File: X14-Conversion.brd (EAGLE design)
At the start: 50.8 x 76.2 mm, 23 parts, among them P1 282837-2, P2 282837-2, P3 282837-2

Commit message: Complete Board Layout
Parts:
- C3: device SparkFun-Capacitors:0402 -> SparkFun-Capacitors:0603
- CB: value 10nF 0Ω -> 10NF-0603-50V-10%
- CONN: value DISTRIBUTION-CONVERSION -> CONVERSION-DISTRIBUTION; device CONN, Distribution-Conversion:TSW-105-05-G-S -> CONN, Distribution-Conversion (3):TSW-105-05-G-S(C-D)
- moved U$7 69.9 mm to (63.0, 44.8)
- moved U$6 67.3 mm to (63.8, 41.5)
- moved U$5 64.1 mm to (63.5, 38.0)
- moved P3 62.9 mm to (7.49, 69.8), turned to 180 degrees
- moved U$4 61.3 mm to (65.2, 28.7)
- moved U$3 61.3 mm to (64.9, 32.0)
- moved U$2 61.1 mm to (64.6, 34.8)
- moved COUT 38.2 mm to (30.6, 32.5), turned to 270 degrees
- moved L1 34.0 mm to (16.9, 33.5)
- moved CINX 31.8 mm to (17.5, 42.3), turned to 270 degrees
- moved AZ1117C 29.7 mm to (15.7, 20.2), flipped to the bottom, turned to 270 degrees
- moved LM2678 29.3 mm to (20.4, 47.6), turned to 90 degrees
- moved CONN 28.1 mm to (42.0, 37.3), flipped to the bottom
- moved CB 28.1 mm to (19.6, 42.3), turned to 270 degrees
- moved D1 27.7 mm to (21.0, 55.6)
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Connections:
- net 12V: now also CONN.2, P3.2; no longer CONN.6, P2.2
- net 3.3V: now also CONN.5, CONN.6; no longer CONN.2, CONN.7
- net 5.2V: now also CONN.7, P2.2; no longer CONN.3, P1.1
- net GND: now also CONN.3, P1.1; no longer CONN.5, P3.2
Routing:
- net N$2: track 0.00 -> 39.9 mm, vias 0 -> 2
- net 3.3V: track 0.00 -> 21.8 mm, vias 0 -> 1
- net 5.2V: track 0.00 -> 3.58 mm
- net N$4: track 0.00 -> 2.68 mm
- net 12V: track 1.05 -> 3.50 mm
- added copper zone on layer 1, net 12V
- added copper zone on layer 16, net 3.3V
- added copper zone on layer 1, net 5.2V
- added copper zone on layer 16, net 5.2V
- added copper zone on layer 1, net GND
- added copper zone on layer 16, net GND
- added copper zone on layer 1, net N$5
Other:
- board text added: "12V"
- board text added: "3.3V"
- board text added: "5.2V"
- board text added: "GND"

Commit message: Completet Board Layout (1)
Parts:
- moved U$5 60.7 mm to (5.08, 54.5)
- moved U$6 44.8 mm to (29.6, 70.5)
- moved U$4 35.7 mm to (38.2, 52.2)
- moved U$3 34.8 mm to (40.0, 7.75)
- moved U$2 31.6 mm to (35.6, 22.5)
- moved U$7 21.1 mm to (42.9, 38.4)
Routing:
- net 3.3V: track 21.8 -> 7.72 mm, vias 1 -> 0
- net 5.2V: track 3.58 -> 2.85 mm

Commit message: Fix Board Layout
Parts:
- removed LM2678: LM2678SD-ADJ/NOPB, LM2678SX-ADJNOPB:SRC14A
- added U1: BUCK,LM2678S-ADJ, BUCK, LM2678S-ADJ:TO127P1435X464-8N
- moved U$6 52.8 mm to (5.84, 23.4)
- moved U$5 28.7 mm to (29.6, 69.3)
- moved D1 7.58 mm to (13.6, 57.4), turned to 90 degrees
- moved U$4 5.60 mm to (37.8, 46.6)
- moved U$7 4.76 mm to (43.7, 33.7)
- moved C3 4.09 mm to (29.3, 44.1)
- moved CB 4.09 mm to (23.2, 44.1)
- moved CINX 4.09 mm to (21.2, 44.1)
- moved RFB1 4.09 mm to (25.3, 44.1)
- moved RFB2 4.09 mm to (27.3, 44.1)
- moved L1 2.08 mm to (15.6, 35.2)
- moved COUT 2.08 mm to (29.3, 34.2)
- moved CIN 1.98 mm to (14.3, 46.2), turned to 180 degrees
- moved U$3 0.72 mm to (39.5, 8.26)
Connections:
- net 12V: now also U1.2; no longer LM2678.3
- net GND: now also U1.4, U1.8; no longer LM2678.15, LM2678.9
- net N$2: now also U1.1; no longer LM2678.14
- net N$4: now also U1.3; no longer LM2678.4
- net N$5: now also U1.6; no longer LM2678.7
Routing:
- net N$5: track 0.00 -> 5.13 mm
- net N$4: track 2.55 -> 3.20 mm
- removed copper zone on layer 1, net N$5

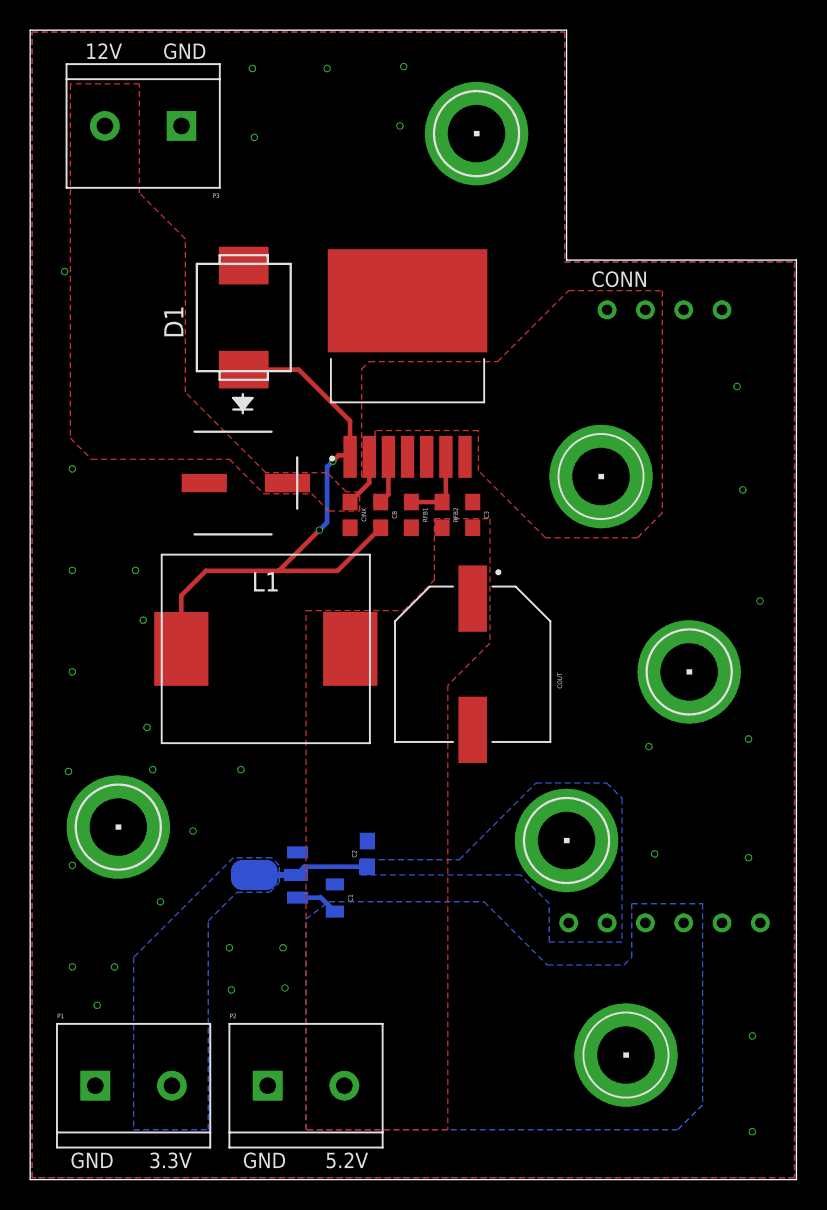
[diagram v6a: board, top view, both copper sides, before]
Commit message: Fix board layout
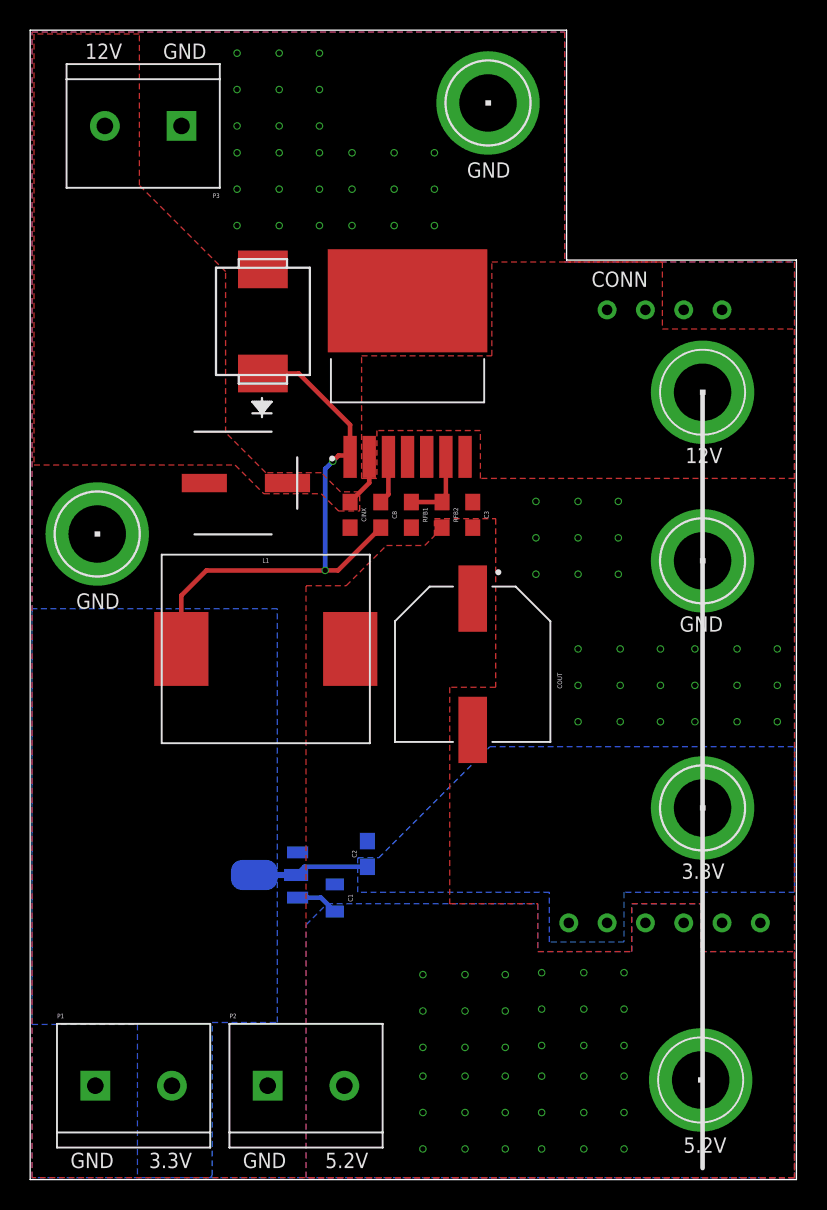
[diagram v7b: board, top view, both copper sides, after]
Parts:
- moved U$6 19.5 mm to (4.45, 42.8)
- moved U$2 9.27 mm to (44.6, 24.6)
- moved U$4 8.75 mm to (44.6, 52.2)
- moved U$7 7.42 mm to (44.6, 41.0)
- moved U$3 5.22 mm to (44.5, 6.60)
- moved U$5 2.17 mm to (30.4, 71.4)
- moved D1 1.30 mm to (14.9, 57.1)
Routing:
- net N$2: track 39.6 -> 36.7 mm
